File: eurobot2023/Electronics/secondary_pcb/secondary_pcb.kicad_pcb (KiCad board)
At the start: 2 copper layers, 74 x 88 mm, 35 parts, among them IC1 CD74HCT125M96, IC2 SN74LVC126ADR, J1 PI40HAT, J2 Conn_01x02_Male, J3 Conn_01x02_Male, J4 Conn_01x02_Male, J5 Conn_01x02_Male, J6 Conn_01x02_Male, P1 R-78Bxx-2.0, P2 Amazon 5A stepdown, U1 MCP2515-xSO, U2 TJA1049T, U4 Pololu_MAX14870

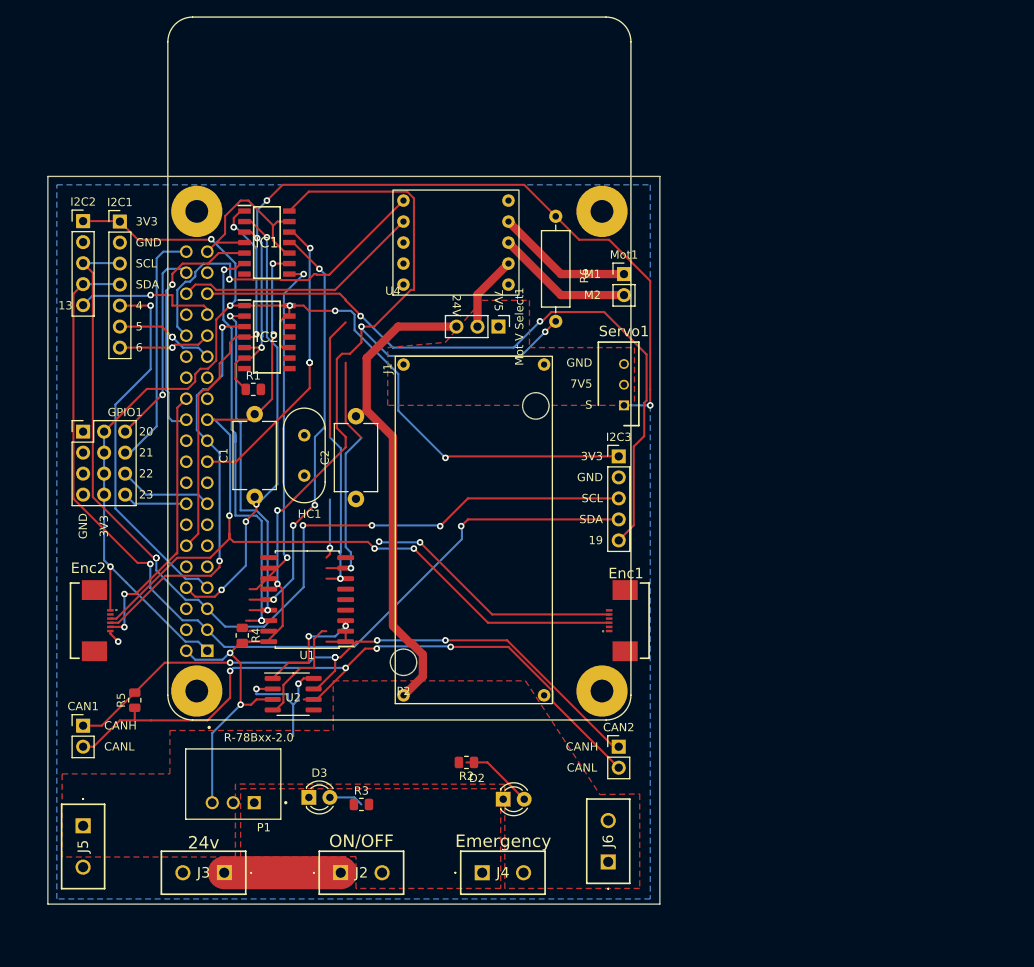
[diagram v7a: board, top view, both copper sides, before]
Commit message: Secondary PCB: full version with DRC ok.
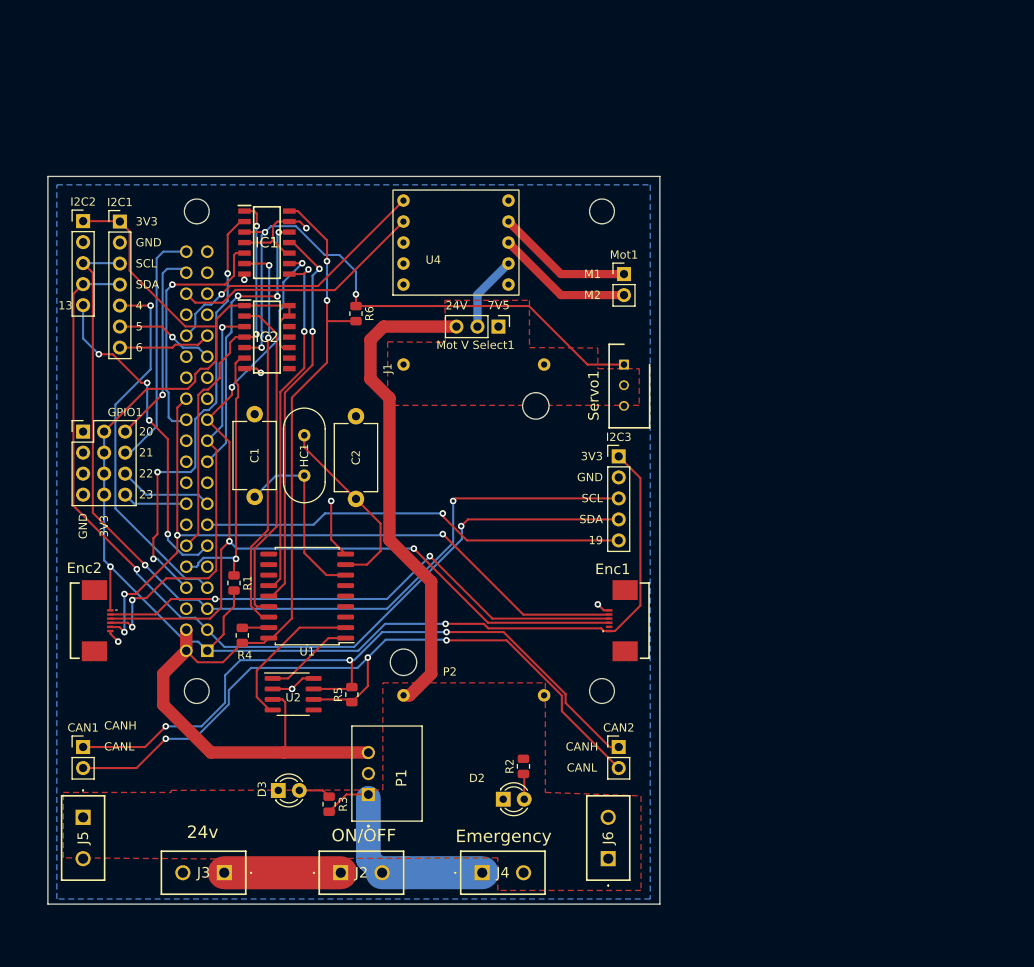
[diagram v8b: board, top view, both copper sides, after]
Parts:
- P1: value R-78Bxx-2.0 -> P1
- R6: footprint Resistor_THT:R_Axial_DIN0309_L9.0mm_D3.2mm_P12.70mm_Horizontal -> Resistor_SMD:R_0805_2012Metric
- moved R6 26.9 mm to (104.8, 72.1)
- moved R5 26.3 mm to (104.2, 118.2)
- moved R1 23.5 mm to (90.0, 104.7), turned to -90 degrees
- moved P1 13.8 mm to (106.2, 130.2), turned to 90 degrees
- moved C1 10.0 mm to (92.5, 84.2), turned to -90 degrees
- moved C2 10.0 mm to (104.8, 84.5), turned to -90 degrees
- moved R2 6.91 mm to (125.0, 126.8), turned to 90 degrees
- moved Servo1 4.94 mm to (137.2, 78.2), turned to 90 degrees
- moved R3 3.91 mm to (101.5, 131.4), turned to -90 degrees
- moved D3 3.79 mm to (95.4, 129.8)
- moved CAN1 2.58 mm to (71.8, 124.5)
- moved J5 1.03 mm to (71.8, 133.0)
- moved U1 0.43 mm to (98.8, 106.2)
- moved J6 0.39 mm to (135.3, 138.0)
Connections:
- R1 pad 2: +5V -> +3.3V
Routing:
- net /GPIO 19: track 83.7 -> 0.00 mm, vias 2 -> 0
- net +5V: track 187.1 -> 117.3 mm, vias 8 -> 2
- net Net-(Enc1-Pad4): track 0.00 -> 66.4 mm, vias 0 -> 2
- net Net-(C2-Pad2): track 86.8 -> 22.7 mm, vias 1 -> 0
- net +24V: track 0.00 -> 58.9 mm
- net /GPIO 27: track 0.00 -> 51.9 mm, vias 0 -> 1
- net /SPI1 CLK_5: track 0.00 -> 42.5 mm, vias 0 -> 2
- net /UART_RX: track 0.00 -> 33.5 mm, vias 0 -> 1
- net +3.3V: track 154.8 -> 183.4 mm, vias 7 -> 2
- net /UART_HalfDuplex: track 99.5 -> 71.8 mm, vias 5 -> 3
- net Net-(J2-Pad2): track 0.35 -> 27.4 mm
- net /SPI1_CS1: track 64.9 -> 89.9 mm
- net /GPIO 17: track 17.6 -> 40.0 mm, vias 1 -> 4
- net GND: track 49.8 -> 30.9 mm, vias 4 -> 7
- net Net-(CAN1-Pad1): track 98.2 -> 86.6 mm, vias 7 -> 3
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- removed copper zone on F.Cu, net Net-(J2-Pad2)
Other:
- board text removed: "S"
